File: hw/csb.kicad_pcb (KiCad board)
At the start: 2 copper layers, 100 x 90 mm, 72 parts, among them J101 AMPSEAL_23_POS_VERT_BLUE_SEAL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, J102 AMPSEAL_8_POS_VERT_BLACK_SEAL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, J1301 ARM_JTAG_SWD_HEADER_10_PINSMD, U1001 ZXCT1086, U1101 ZXCT1086, U1201 ZXCT1086, U1301 LPC1549JBD64, U1302 MCP2551_SOIC8, U301 MOSFET_DRIVER_LT1161, U302 MOSFET_IPG20N04S4L11ATMA1, U303 MOSFET_IPG20N04S4L11ATMA1, U304 MOSFET_IPG20N04S4L11ATMA1, U401 ZXCT1086, U501 ZXCT1086, U601 ZXCT1086, U701 ZXCT1086, U801 MOSFET_DRIVER_LT1161, U802 MOSFET_IPG20N04S4L11ATMA1, U803 MOSFET_IPG20N04S4L11ATMA1, U804 MOSFET_IPG20N04S4L11ATMA1, U805 MOSFET_IPG20N04S4L11ATMA1, U901 ZXCT1086, X1301 XTAL_7A-12.000MAAJ-T

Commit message: 3.1.0 hw created, not yet ordered
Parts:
- removed C1301, C1302, C1303, C1304, C1305, C1306, C1309, C801, C802, C803, C804, C805, C806: 100nF, kemet:0603
- removed C1307, C1308: 18pF, kemet:0603
- removed J1301: ARM_JTAG_SWD_HEADER_10_PINSMD, usevolt:ARM_10_PIN_JTAG_SWD_CONNECTOR
- removed R1001, R1101: LRMAT2512-R002FT4, usevolt:2512
- removed R1201: LRMAT2512-R004FT4, usevolt:2512
- removed R1301, R1302, R1303, R1304: 10K, multicomp:0603
- removed U1001, U1101, U1201: ZXCT1086, usevolt:SOT-25
- removed U1301: LPC1549JBD64, usevolt:QFP64
- removed U1302: MCP2551_SOIC8, usevolt:SOIC8
- removed U303, U304, U802, U803, U804, U805: MOSFET_IPG20N04S4L11ATMA1, usevolt:PG-TDSON-8-4
- removed X1301: XTAL_7A-12.000MAAJ-T, usevolt:XTAL_7A-20.000MAJ
- added C307: 18pF, kemet:0603, F.Cu at (139.2, 55.5)
- added C308: 18pF, kemet:0603, F.Cu at (135.7, 55.5)
- added C309: 100nF, kemet:0603, F.Cu at (131.8, 115.8)
- added D204: SCHOTTKY_DIODE_V40PW10C, usevolt:SlimDPAK, F.Cu at (182.6, 121.5)
- added D205: SCHOTTKY_DIODE_V40PW10C, usevolt:SlimDPAK, F.Cu at (153.3, 121.5)
- added D206: DIODE_TVS_TPSMD28A, usevolt:DO-214AB, F.Cu at (168.0, 112.1)
- added J301: ARM_JTAG_SWD_HEADER_10_PINSMD, usevolt:ARM_10_PIN_JTAG_SWD_CONNECTOR, F.Cu at (126.8, 56.2)
- added R302: 10K, multicomp:0603, F.Cu at (142.7, 63.3)
- added R303: 10K, multicomp:0603, F.Cu at (128.5, 51.9)
- added R304: 10K, multicomp:0603, F.Cu at (125.1, 51.9)
- added R402: 390, yageo:0603, F.Cu at (167.2, 103.5)
- added R403: 1K, yageo:0603, F.Cu at (164.1, 103.5)
- added R404: 1K, yageo:0603, F.Cu at (162.4, 103.5)
- added R502: 1K, yageo:0603, F.Cu at (149.7, 87.5)
- added R602: 1K, yageo:0603, F.Cu at (157.3, 87.5)
- added R702: 1K, yageo:0603, F.Cu at (179.2, 87.5)
- added R802: 1K, yageo:0603, F.Cu at (186.9, 87.5)
- added R902: 390, yageo:0603, F.Cu at (173.7, 103.5)
- added R903: 1K, yageo:0603, F.Cu at (170.4, 103.5)
- added R904: 1K, yageo:0603, F.Cu at (168.8, 103.5)
- added X301: XTAL_7A-12.000MAAJ-T, usevolt:XTAL_7A-20.000MAJ, F.Cu at (137.5, 52.7)
- C202: value T491D226K035AT -> CAP_EEE-FK1H470P; footprint kemet:7343 -> usevolt:CAP_EEE-FK1H470P
- R301: value R_ARRAY4_1K -> 10K; footprint usevolt:0603_array4 -> multicomp:0603
- R401: value LRMAM1206-R015FT5 -> 390; footprint usevolt:1206 -> yageo:0603
- R501, R701: value LRMAT2512-R004FT4 -> 560; footprint usevolt:2512 -> yageo:0603
- R601: value LRMAM1206-R015FT5 -> 560; footprint usevolt:1206 -> yageo:0603
- R801: value R_ARRAY4_1K -> 560; footprint usevolt:0603_array4 -> yageo:0603
- R901: value LRMAT2512-R002FT4 -> 390; footprint usevolt:2512 -> yageo:0603
- U301: value MOSFET_DRIVER_LT1161 -> LPC1549JBD64; footprint usevolt:SO20 -> usevolt:QFP64
- U302: value MOSFET_IPG20N04S4L11ATMA1 -> MCP2551_SOIC8; footprint usevolt:PG-TDSON-8-4 -> usevolt:SOIC8
- U401, U901: value ZXCT1086 -> VND5050AJTR-E; footprint usevolt:SOT-25 -> usevolt:PowerSSO-12
- U501, U601, U701: value ZXCT1086 -> BTS6133D; footprint usevolt:SOT-25 -> usevolt:DPAK-5
- U801: value MOSFET_DRIVER_LT1161 -> BTS6133D; footprint usevolt:SO20 -> usevolt:DPAK-5
- moved U401 91.5 mm to (165.2, 97.9), turned to 0 degrees
- moved U501 82.6 mm to (149.7, 96.8), turned to 180 degrees
- moved U601 74.4 mm to (157.3, 96.8), turned to 180 degrees
- moved U901 72.8 mm to (170.7, 97.9), turned to 0 degrees
- moved U701 53.3 mm to (179.4, 96.8), turned to 180 degrees
- moved R701 35.1 mm to (178.7, 89.2), turned to 0 degrees
- moved C304 34.9 mm to (132.4, 57.7), turned to 90 degrees
- moved U302 30.3 mm to (136.3, 116.0), turned to 0 degrees
- moved R801 27.5 mm to (186.4, 89.2), turned to 0 degrees
- moved R301 25.7 mm to (142.7, 65.1), turned to 180 degrees
- moved C303 24.4 mm to (120.5, 66.7), turned to 180 degrees
- moved C305 22.1 mm to (137.8, 72.2)
- moved R601 21.1 mm to (156.7, 89.2), turned to 0 degrees
- moved R501 20.0 mm to (149.1, 89.2), turned to 0 degrees
- moved U801 19.7 mm to (186.9, 96.8), turned to 180 degrees
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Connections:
- C301 pad 1: GND -> +3V3
- C301 pad 2: Net-(C301-Pad2) -> GND
- C302 pad 1: GND -> +3V3
- C302 pad 2: Net-(C302-Pad2) -> GND
- C303 pad 1: GND -> +3V3
- C303 pad 2: Net-(C303-Pad2) -> GND
- C304 pad 1: GND -> +3V3
- C304 pad 2: Net-(C304-Pad2) -> GND
- C305 pad 1: VDD -> +3V3
- C306 pad 1: VDD -> +3V3
- D201 pad P$1: VDD -> /Power Supply/VIN
- J101 pad P$1: (no net) -> /DRIVE_15A
- J101 pad P$11: (no net) -> /WORK_15A
- J101 pad P$2: (no net) -> /DRIVE_15A
- J101 pad P$3: (no net) -> /WORK_15A
- J102 pad P$1: VDD -> /Power Supply/VIN
- J102 pad P$3: VDD -> /Power Supply/VIN
- J102 pad P$6: VDD -> /Power Supply/VIN
- R301 pad 1: /BEACON -> /LPC1549/WIPER_POS
- R301 pad 2: GND -> Net-(R301-Pad2)
- R401 pad 1: /LT1161/sheet58BE8E45/SENSE- -> /LPC1549/BACK_SENSE
- R401 pad 2: VDD -> GND
- R501 pad 1: /LT1161/sheet58BE8E46/SENSE- -> /LPC1549/DRIVE_SENSE
- R501 pad 2: VDD -> GND
- R601 pad 1: /LT1161/sheet58BE8E47/SENSE- -> /Sheet5A019745/SENSE1
- R601 pad 2: VDD -> GND
- R701 pad 1: /LT1161/sheet58BE8E48/SENSE- -> /LPC1549/OILCOOLER_SENSE
- R701 pad 2: VDD -> GND
- R801 pad 1: /WIPER -> /LPC1549/COOLER_SENSE
- R901 pad 1: /LT1161_2/sheet58BE8E45/SENSE- -> /LPC1549/IN_SENSE
- R901 pad 2: VDD -> GND
- U302 pad 1: /WORK_15A -> /LPC1549/CAN_TX
- U302 pad 2: Net-(U301-Pad12) -> GND
- U302 pad 3: /WORK_15A -> +5V
- U302 pad 4: Net-(U301-Pad12) -> /LPC1549/CAN_RX
- U302 pad 5: /LT1161/sheet58BE8E48/SENSE- -> (no net)
- U302 pad 6: /LT1161/sheet58BE8E48/SENSE- -> /CANL
- U401 pad 1: /BEACON_SENSE -> GND
- U401 pad 2: GND -> /LPC1549/BEACON
- U401 pad 3: VDD -> /LPC1549/BACK
- U401 pad 4: /LT1161/sheet58BE8E45/SENSE- -> /LPC1549/BACK_SENSE
- U401 pad 5: +3V3 -> /LPC1549/BEACON_SENSE
- U501 pad 1: /DRIVE_SENSE -> /DRIVE_15A
- U501 pad 2: GND -> /LPC1549/DRIVE
- U501 pad 3: VDD -> /LPC1549/DRIVE_SENSE
- U501 pad 4: /LT1161/sheet58BE8E46/SENSE- -> /DRIVE_15A
- U501 pad 5: +3V3 -> VDD
- U601 pad 1: /BACK_SENSE -> /WORK_15A
- U601 pad 2: GND -> /Sheet5A019745/IN1
- U601 pad 3: VDD -> /Sheet5A019745/SENSE1
- U601 pad 4: /LT1161/sheet58BE8E47/SENSE- -> /WORK_15A
- U601 pad 5: +3V3 -> VDD
- U701 pad 1: /WORK_SENSE -> /COOLER_30A
- U701 pad 2: GND -> /Sheet5A01A444/IN1
- U701 pad 3: VDD -> /LPC1549/OILCOOLER_SENSE
- U701 pad 4: /LT1161/sheet58BE8E48/SENSE- -> /COOLER_30A
- U701 pad 5: +3V3 -> VDD
- U801 pad 1: GND -> /OILCOOLER_15A
- U801 pad 2: Net-(C801-Pad2) -> /LPC1549/COOLER
- U801 pad 3: /WIPER -> /LPC1549/COOLER_SENSE
- U801 pad 4: Net-(C802-Pad2) -> /OILCOOLER_15A
- U801 pad 5: /IN -> VDD
- U901 pad 1: /WIPER_SENSE -> GND
- U901 pad 2: GND -> /Sheet5A02A41E/IN2
- U901 pad 3: VDD -> /LPC1549/IN
- U901 pad 4: /LT1161_2/sheet58BE8E45/SENSE- -> /LPC1549/IN_SENSE
- U901 pad 5: +3V3 -> /Sheet5A02A41E/SENSE2
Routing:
- net (no net): track 774.6 -> 0.00 mm, vias 45 -> 0
- net GND: track 503.0 -> 1015.2 mm, vias 46 -> 96
- net VDD: track 277.0 -> 0.00 mm, vias 10 -> 0
- net /BACK: track 222.1 -> 0.00 mm, vias 14 -> 0
- net Net-(C801-Pad2): track 117.6 -> 0.00 mm, vias 14 -> 0
- net /LT1161_2/sheet58BE8E45/SENSE-: track 112.0 -> 0.00 mm, vias 4 -> 0
- net /OILCOOLER_SENSE: track 104.8 -> 0.00 mm, vias 4 -> 0
- net /IN_SENSE: track 102.3 -> 0.00 mm, vias 4 -> 0
- net /COOLER_SENSE: track 100.1 -> 0.00 mm, vias 4 -> 0
- net +3V3: track 242.0 -> 143.6 mm, vias 4 -> 0
- net /LPC1549/COOLER: track 0.00 -> 80.2 mm, vias 0 -> 2
- net /Sheet5A02A41E/SENSE2: track 0.00 -> 78.0 mm, vias 0 -> 2
- net /LPC1549/COOLER_SENSE: track 0.00 -> 77.1 mm, vias 0 -> 2
- net /LPC1549/IN_SENSE: track 0.00 -> 75.0 mm, vias 0 -> 2
- net /Sheet5A01A444/IN1: track 0.00 -> 72.5 mm, vias 0 -> 2
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- added copper zone on F.Cu, net /COOLER_30A
- added copper zone on F.Cu, net /DRIVE_15A
- added copper zone on F.Cu, net /Power Supply/VIN
- added copper zone on F.Cu, net /WORK_15A
- removed copper zone on F.Cu, net /LT1161_2/Sheet59847684/SENSE-

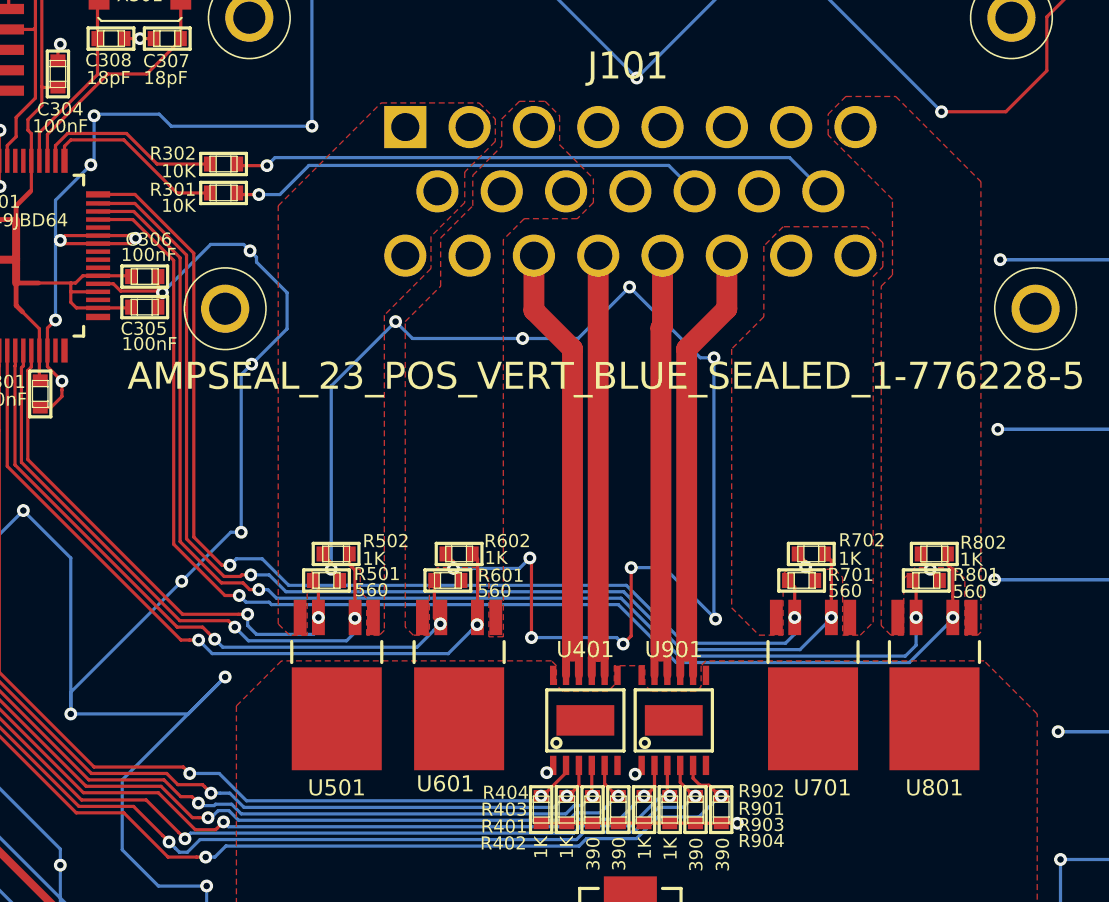
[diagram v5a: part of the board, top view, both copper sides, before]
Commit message: oil cooler removed, 3.2.0 ready to order
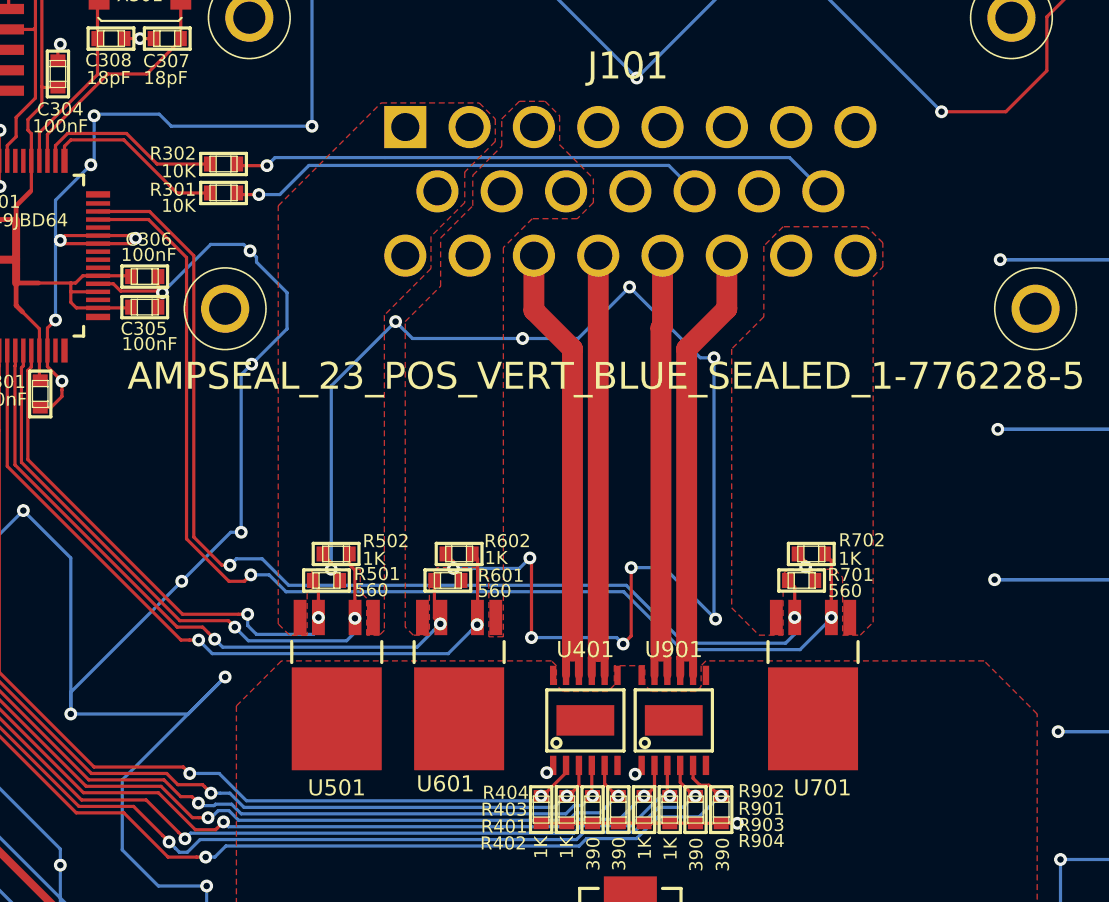
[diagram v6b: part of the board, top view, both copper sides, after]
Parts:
- removed R801: 560, yageo:0603
- removed R802: 1K, yageo:0603
- removed U801: BTS6133D, usevolt:DPAK-5
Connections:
- J101 pad P$8: /OILCOOLER_15A -> (no net)
- R701 pad 1: /LPC1549/OILCOOLER_SENSE -> /LPC1549/COOLER_SENSE
- R702 pad 2: /Sheet5A01A444/IN1 -> /LPC1549/COOLER
- U301 pad P$31: /Sheet5A01A444/IN1 -> (no net)
- U301 pad P$32: /LPC1549/OILCOOLER_SENSE -> (no net)
- U701 pad 2: /Sheet5A01A444/IN1 -> /LPC1549/COOLER
- U701 pad 3: /LPC1549/OILCOOLER_SENSE -> /LPC1549/COOLER_SENSE
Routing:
- net /Sheet5A01A444/IN1: track 72.5 -> 0.00 mm, vias 2 -> 0
- net /LPC1549/OILCOOLER_SENSE: track 69.3 -> 0.00 mm, vias 2 -> 0
- net /LPC1549/COOLER_SENSE: track 77.1 -> 68.8 mm
- net /LPC1549/COOLER: track 80.2 -> 72.2 mm
- net GND: track 1015.2 -> 1013.0 mm, vias 96 -> 95
- removed copper zone on F.Cu, net /OILCOOLER_15A

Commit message: hw 3.3 created
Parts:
- R501, R601, R701: value 560 -> 1K
- R502, R602, R702: value 1K -> 390
- U501, U601, U701: value BTS6133D -> VN5E010AH; footprint usevolt:DPAK-5 -> usevolt:HPAK
- moved U501 1.21 mm to (149.6, 98.0)
- moved U701 1.20 mm to (179.3, 98.0)
- moved U601 1.20 mm to (157.3, 98.0)
- moved R701 1.01 mm to (179.7, 89.3)
- moved R601 0.95 mm to (157.6, 89.2)
- moved R501 0.75 mm to (149.8, 89.2)
- moved R502 0.35 mm to (149.3, 87.5)
- moved R602 0.25 mm to (157.1, 87.5)
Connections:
- R501 pad 1: /LPC1549/DRIVE_SENSE -> GND
- R501 pad 2: GND -> /LPC1549/DRIVE
- R502 pad 1: GND -> /LPC1549/DRIVE_SENSE
- R502 pad 2: /LPC1549/DRIVE -> GND
- R601 pad 1: /Sheet5A019745/SENSE1 -> GND
- R601 pad 2: GND -> /Sheet5A019745/IN1
- R602 pad 1: GND -> /Sheet5A019745/SENSE1
- R602 pad 2: /Sheet5A019745/IN1 -> GND
- R701 pad 1: /LPC1549/COOLER_SENSE -> GND
- R701 pad 2: GND -> /LPC1549/COOLER
- R702 pad 1: GND -> /LPC1549/COOLER_SENSE
- R702 pad 2: /LPC1549/COOLER -> GND
- U501 pad 2: /LPC1549/DRIVE -> GND
- U501 pad 3: /LPC1549/DRIVE_SENSE -> /LPC1549/DRIVE
- U501 pad 4: /DRIVE_15A -> VDD
- U501 pad 5: VDD -> /LPC1549/DRIVE_SENSE
- U601 pad 2: /Sheet5A019745/IN1 -> GND
- U601 pad 3: /Sheet5A019745/SENSE1 -> /Sheet5A019745/IN1
- U601 pad 4: /WORK_15A -> VDD
- U601 pad 5: VDD -> /Sheet5A019745/SENSE1
- U701 pad 2: /LPC1549/COOLER -> GND
- U701 pad 3: /LPC1549/COOLER_SENSE -> /LPC1549/COOLER
- U701 pad 4: /COOLER_30A -> VDD
- U701 pad 5: VDD -> /LPC1549/COOLER_SENSE
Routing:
- net GND: track 1013.0 -> 1021.5 mm, vias 95 -> 99
- net /Sheet5A019745/SENSE1: track 41.7 -> 46.5 mm
- net /LPC1549/DRIVE: track 37.6 -> 35.8 mm
- net /LPC1549/COOLER: track 72.2 -> 70.5 mm
- net /LPC1549/COOLER_SENSE: track 68.8 -> 70.5 mm
- net /LPC1549/DRIVE_SENSE: track 33.2 -> 34.8 mm
